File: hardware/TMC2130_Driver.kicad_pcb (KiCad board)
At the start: 2 copper layers, 36.7 x 39.4 mm, 33 parts, among them J1 PCIe_Stepper, J2 Conn_01x04_Male, J3 Screw_Terminal_01x02, U1 TMC5130, U2 74LVC1G06, U3 24LC02

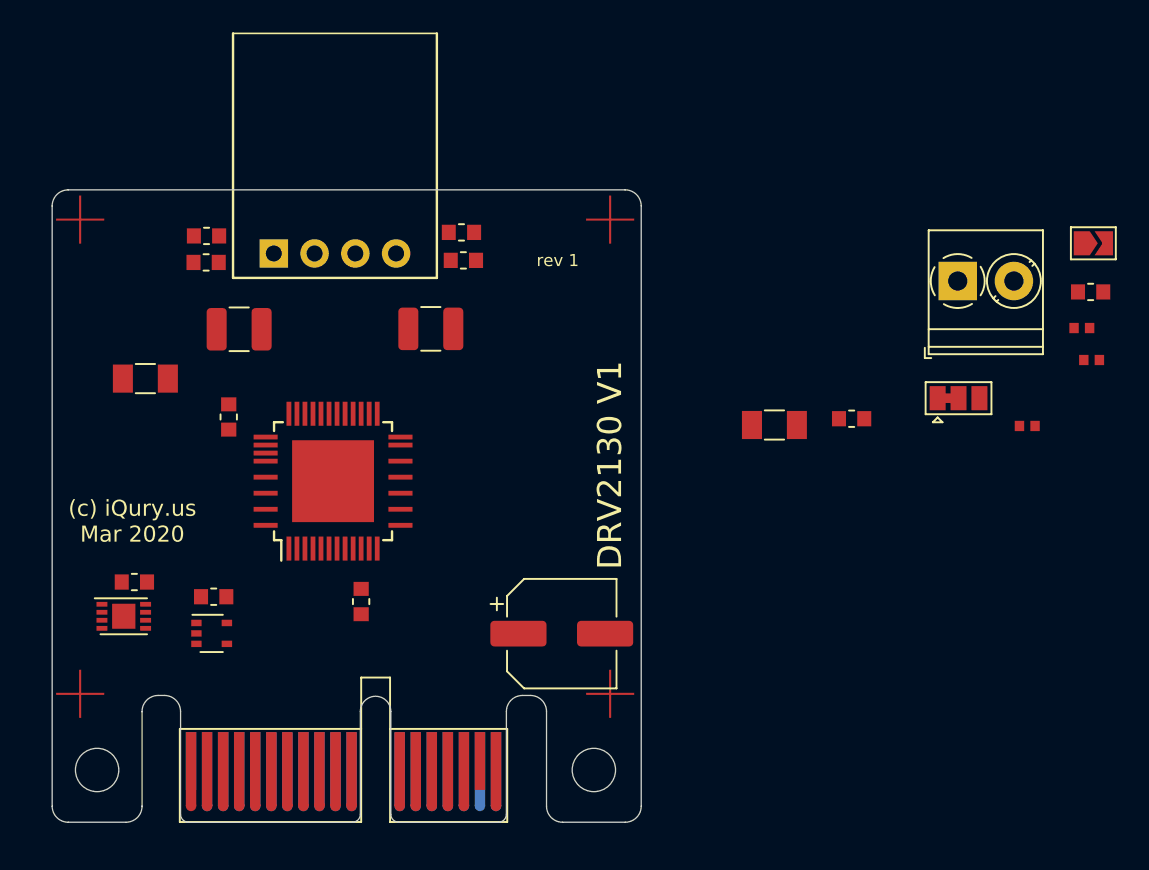
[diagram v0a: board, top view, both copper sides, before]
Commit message: Route the 2130 driver board.
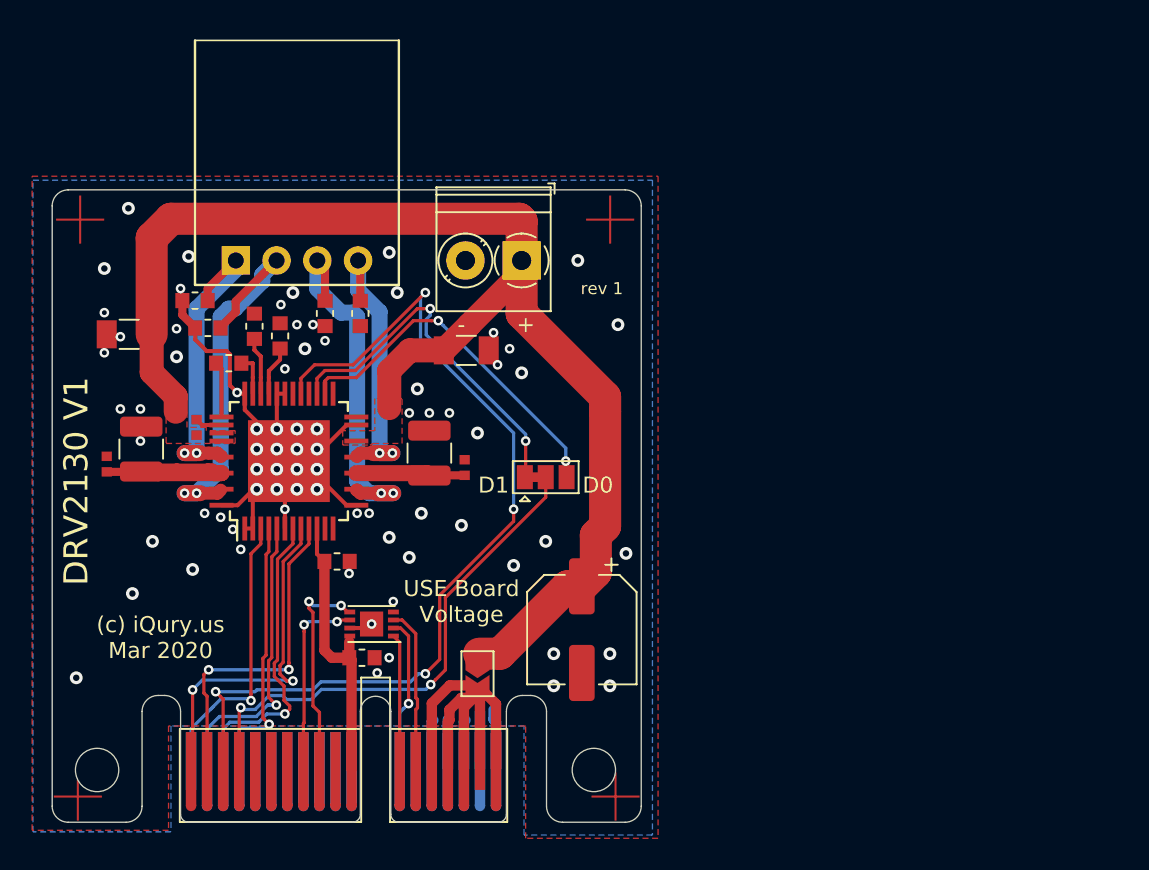
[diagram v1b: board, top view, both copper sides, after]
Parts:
- removed C1: 0.1uF, PrntrBoardV2:C_0603_1608Metric
- removed U2: 74LVC1G06, Package_TO_SOT_SMD:SOT-353_SC-70-5
- moved C15 61.7 mm to (112.4, 91.7), turned to 90 degrees
- moved C9 55.5 mm to (118.0, 89.4), turned to 90 degrees
- moved C8 52.1 mm to (121.6, 83.1), turned to 90 degrees
- moved JP2 46.8 mm to (135.5, 104.8), turned to 270 degrees
- moved C7 36.0 mm to (123.2, 83.7), turned to 270 degrees
- moved C10 35.1 mm to (134.7, 91.9), turned to 90 degrees
- moved J3 27.2 mm to (138.2, 79.0), turned to 180 degrees
- moved LOGO1 26.4 mm to (114.0, 100.2)
- moved JP1 26.2 mm to (139.8, 92.5)
- moved C2 19.8 mm to (134.8, 84.6)
- moved C13 16.9 mm to (117.9, 81.5), turned to 0 degrees
- moved C11 16.9 mm to (118.7, 83.2), turned to 0 degrees
- moved U3 15.4 mm to (128.9, 101.7), turned to 180 degrees
- moved C16 14.9 mm to (128.3, 103.8), turned to 0 degrees
- moved C14 10.1 mm to (128.2, 82.3), turned to 90 degrees
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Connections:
- net Net-(C2-Pad1) renamed /V_HIGH
- C9 pad 2: (no net) -> Net-(C9-Pad2)
- J2 pad 1: /MOTB2 -> /MOTA2
- J2 pad 2: /MOTB1 -> /MOTA1
- J2 pad 3: /MOTA1 -> /MOTB1
- J2 pad 4: /MOTA2 -> /MOTB2
- JP1 pad 2: /DIAG -> /ALARM1
- U1 pad 13: Net-(U1-Pad13) -> GND
- U1 pad 32: Net-(U1-Pad13) -> GND
- U1 pad 38: (no net) -> Net-(C9-Pad2)
- U1 pad 48: Net-(U1-Pad13) -> GND
- U1 pad 49: Net-(U1-Pad13) -> GND
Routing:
- net /V_HIGH: track 0.00 -> 82.4 mm
- net GND: track 0.00 -> 62.5 mm, vias 0 -> 76
- net /~ENABLE: track 0.00 -> 58.0 mm, vias 0 -> 4
- net /ALARM1: track 0.00 -> 32.5 mm, vias 0 -> 2
- net /V_MOTORS: track 0.00 -> 27.7 mm
- net /MOTA1: track 0.00 -> 25.7 mm, vias 0 -> 2
- net Net-(JP1-Pad1): track 0.00 -> 23.0 mm, vias 0 -> 2
- net /MOTB1: track 0.00 -> 22.9 mm, vias 0 -> 2
- net Net-(JP1-Pad3): track 0.00 -> 22.5 mm, vias 0 -> 2
- net /STEP: track 0.00 -> 22.1 mm, vias 0 -> 2
- net /DIR: track 0.00 -> 20.7 mm, vias 0 -> 2
- net /MOTA2: track 0.00 -> 19.6 mm, vias 0 -> 2
- net /MISO: track 0.00 -> 19.3 mm, vias 0 -> 1
- net /MOSI: track 0.00 -> 18.8 mm, vias 0 -> 1
- net /MOTB2: track 0.00 -> 18.3 mm, vias 0 -> 2
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- added copper zone on F.Cu, net /V_HIGH
- added copper zone on B.Cu, net GND
- added copper zone on F.Cu, net GND
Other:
- board text added: "+"
- board text added: "+ -"
- board text added: "-"
- board text added: "12-42V DC"
- board text added: "D0"
- board text added: "D1"
- board text added: "USE Board Voltage"

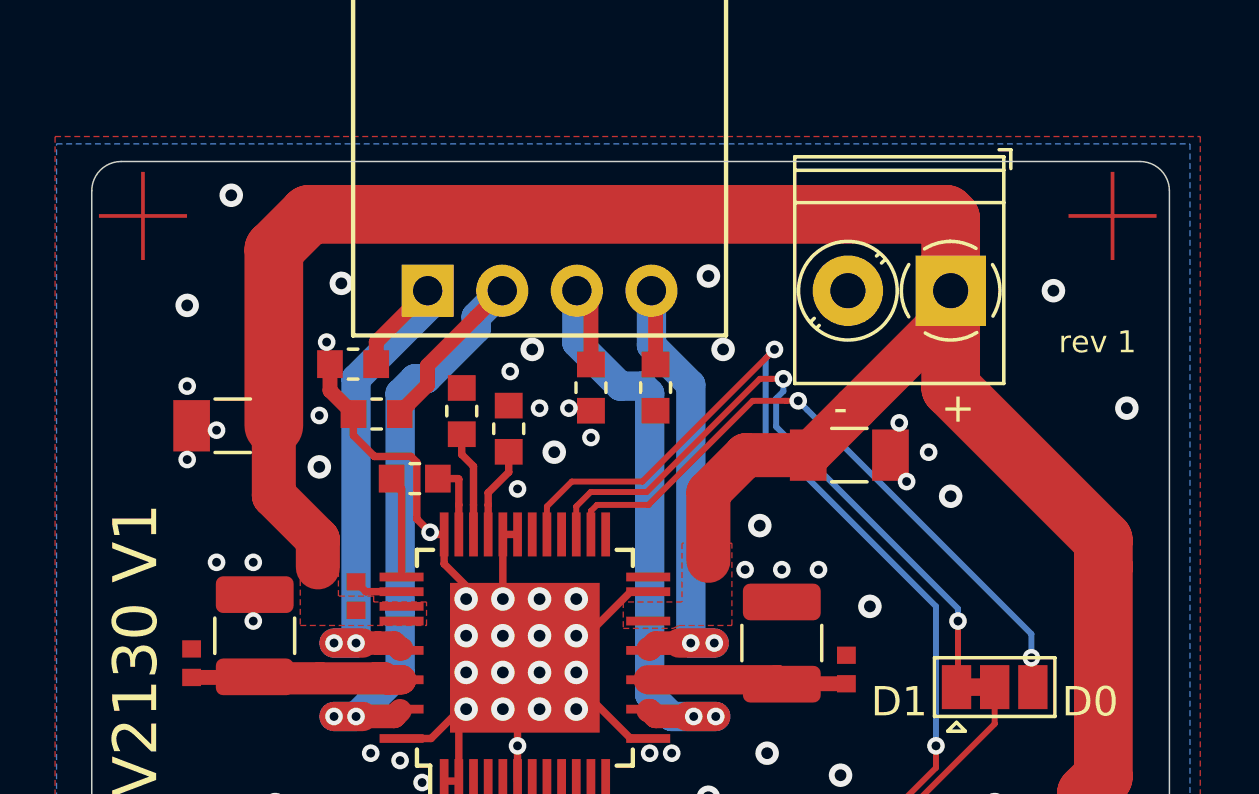
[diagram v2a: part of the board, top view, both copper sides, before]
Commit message: Added power protection to the 2130 driver.
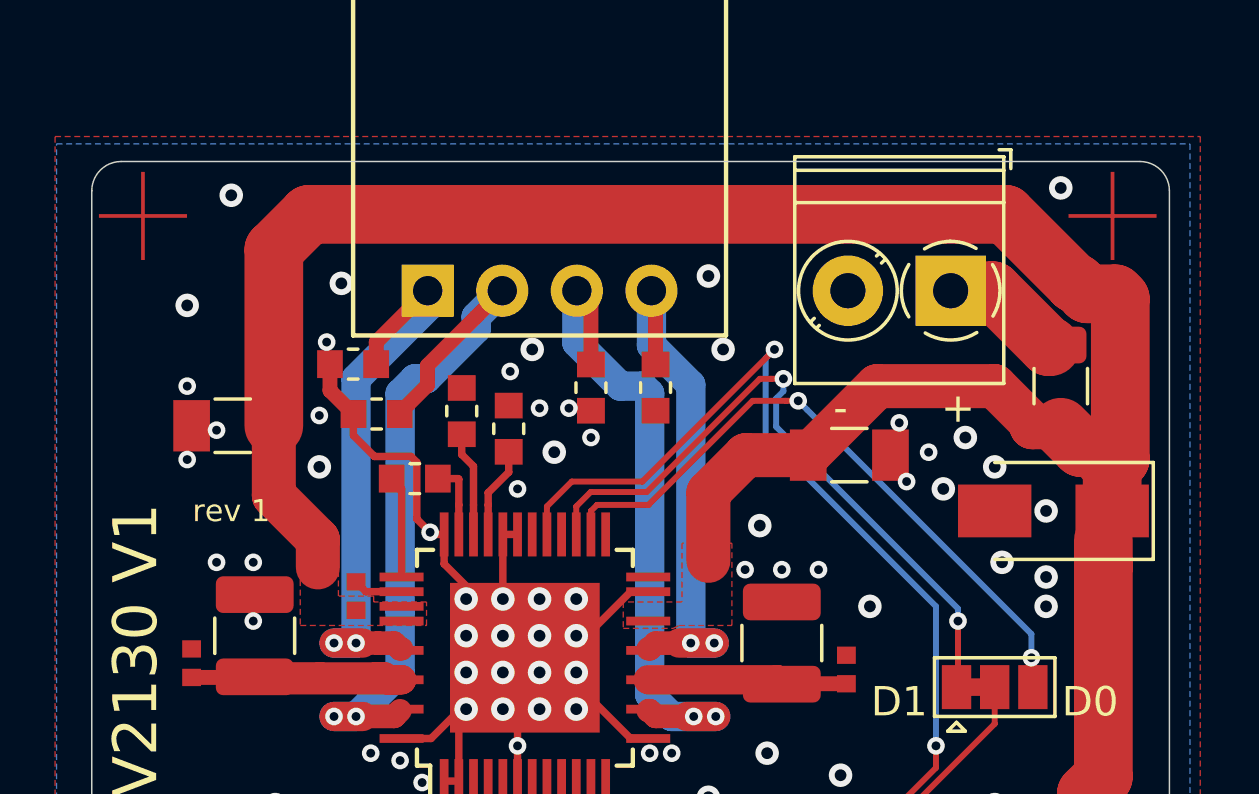
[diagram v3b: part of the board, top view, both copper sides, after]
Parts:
- added D1: SBRT5A50SA, Diode_SMD:D_SMA, F.Cu at (141.8, 86.5)
- added F1: 3A, Fuse:Fuse_1206_3216Metric, F.Cu at (142.0, 82.2)
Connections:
- J3 pad 1: /V_HIGH -> Net-(F1-Pad1)
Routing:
- net /V_HIGH: track 82.4 -> 89.2 mm
- net Net-(F1-Pad1): track 0.00 -> 4.19 mm
- net GND: vias 76 -> 81

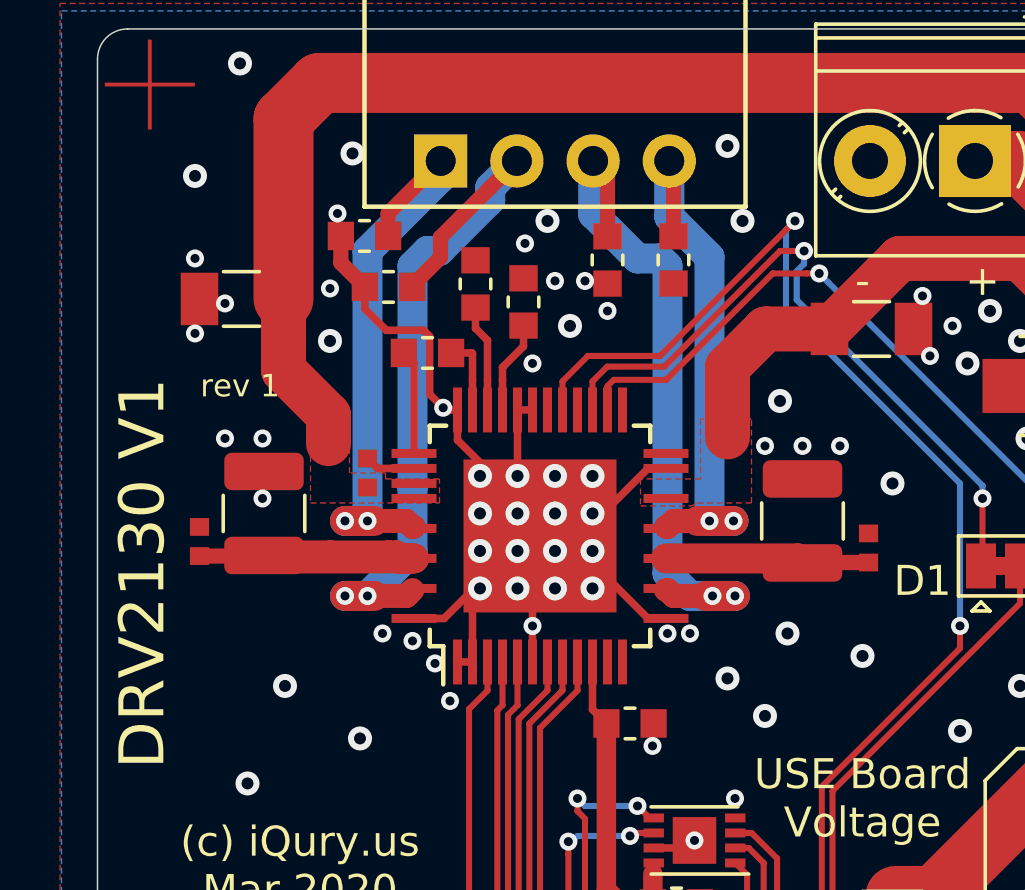
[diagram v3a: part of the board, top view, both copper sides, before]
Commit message: Generate fabrication files for the 2130 driver. Set all JPCPCB properties.
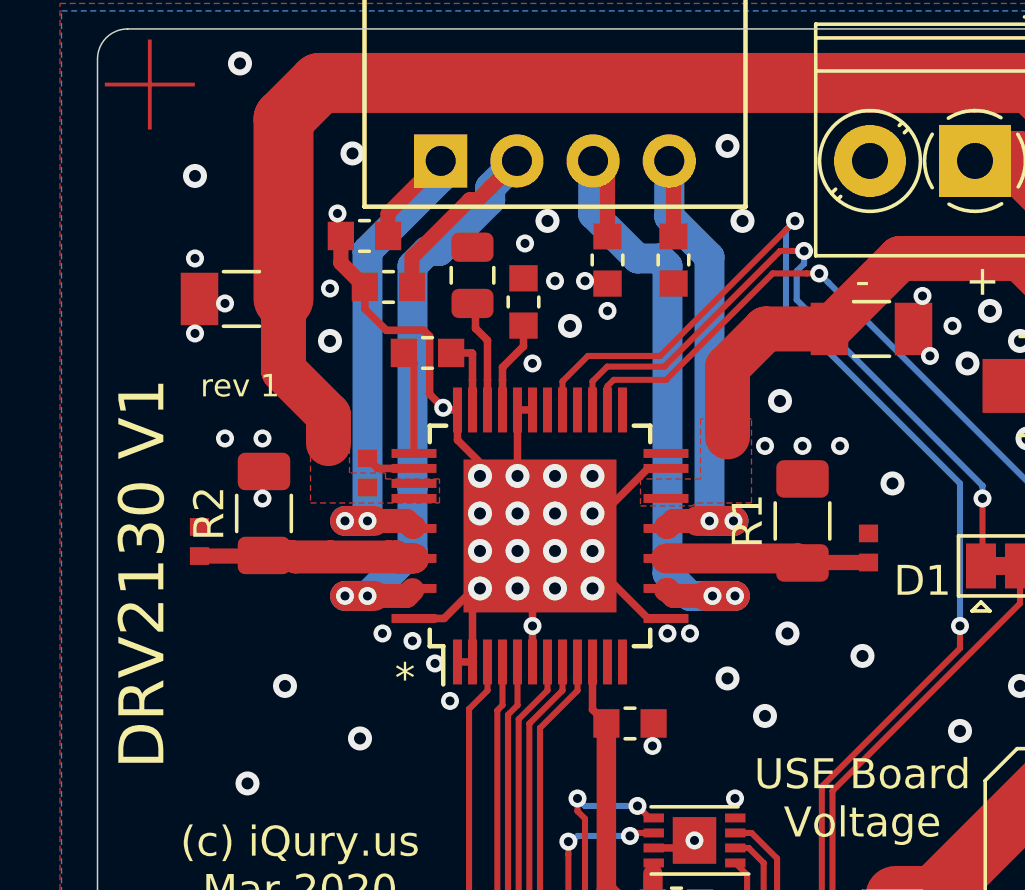
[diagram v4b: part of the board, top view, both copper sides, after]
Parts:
- C8: footprint PrntrBoardV2:C_0603_1608Metric -> Capacitor_SMD:C_0805_2012Metric
- R1, R2: footprint Resistor_SMD:R_1210_3225Metric -> Resistor_SMD:R_1206_3216Metric
- moved C8 0.30 mm to (121.5, 82.8)
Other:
- board text added: "*"

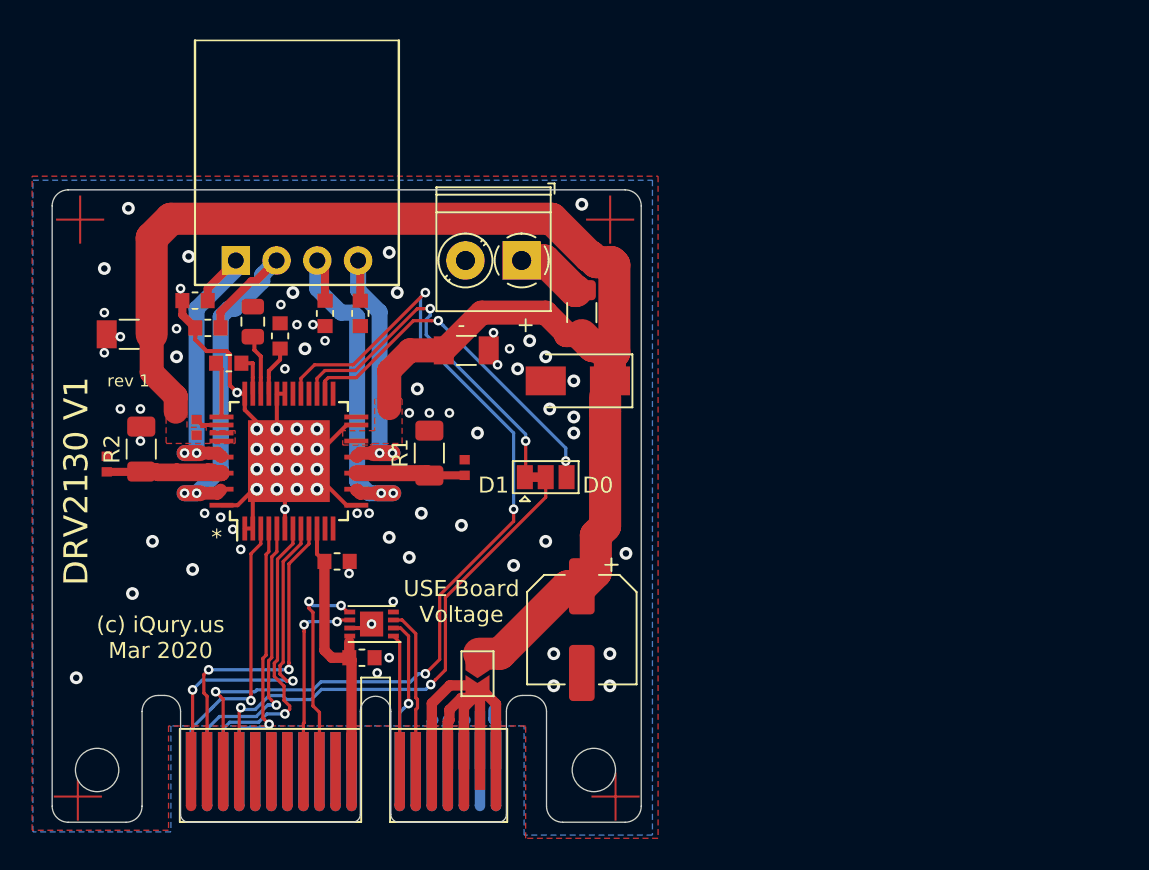
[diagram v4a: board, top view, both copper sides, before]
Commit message: Fix DRC warnings. Update U3 metadata.
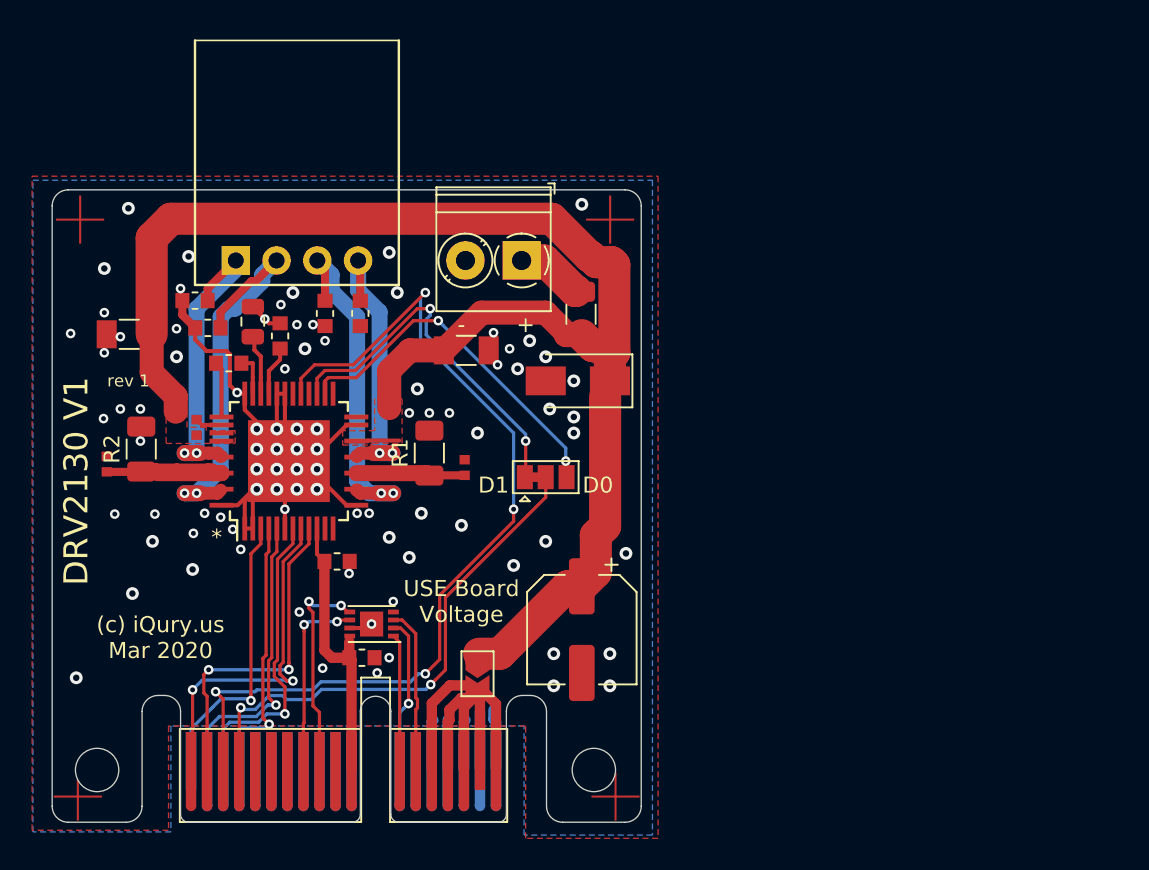
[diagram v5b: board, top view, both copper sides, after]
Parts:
- moved F1 0.11 mm to (141.9, 82.3)
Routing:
- net GND: track 62.5 -> 71.7 mm, vias 81 -> 89
- net /V_HIGH: track 89.2 -> 91.9 mm

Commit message: U3->U2
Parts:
- U1: value TMC5130 -> TMC2130
- renumbered U3 to U2

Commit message: Re generate the tmc2130 gerber files.
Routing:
- added copper zone on F.Cu, net /V_MOTORS
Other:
- board text added: "(c) iQury.us Apt 2020"
- board text removed: "(c) iQury.us Mar 2020"
